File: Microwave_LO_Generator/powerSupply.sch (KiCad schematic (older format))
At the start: 26 parts, among them IC1 ADP150AUJZ-3.3-R7, U2 LM317L_SO8, U3 LM317L_SO8

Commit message: add vco
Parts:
- gave numbers to parts that had none: 3
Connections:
- net labels added: +5VA
- net labels removed: +5V
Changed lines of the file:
@@
 $Descr A4 11693 8268
 encoding utf-8
-Sheet 3 3
+Sheet 3 4
 Title ""
 Date ""
@@
 Wire Wire Line
 	5350 2000 5600 2000
-Wire Wire Line
-	5600 2000 5600 1950
 Connection ~ 5350 2000
 $Comp
@@
 	5600 3950 5600 3900
 Connection ~ 5350 3950
-$Comp
-L power:+5V #PWR0130
-U 1 1 5FC0CF33
-P 5600 1950
-F 0 "#PWR0130" H 5600 1800 50  0001 C CNN
-F 1 "+5V" H 5615 2123 50  0000 C CNN
-F 2 "" H 5600 1950 50  0001 C CNN
-F 3 "" H 5600 1950 50  0001 C CNN
-	1    5600 1950
-	1    0    0    -1
-$EndComp
 Wire Wire Line
 	1600 3600 1600 2000
@@
 AR Path="/5FBFBF42/5FC33DC2" Ref="C?"  Part="1"
 AR Path="/5FBD30A7/5FBFBF42/5FC33DC2" Ref="C?"  Part="1"
-AR Path="/5FBD5B32/5FC33DC2" Ref="C?"  Part="1"
-F 0 "C?" H 9535 2054 50  0000 R CNN
+AR Path="/5FBD5B32/5FC33DC2" Ref="C25"  Part="1"
+F 0 "C25" H 9535 2054 50  0000 R CNN
 F 1 "1u" H 9535 2145 50  0000 R CNN
 F 2 "Capacitor_SMD:C_0402_1005Metric_Pad0.74x0.62mm_HandSolder" H 9688 1950 50  0001 C CNN
@@
 $EndComp
 $Comp
-L pspice:0 #GND?
+L pspice:0 #GND0113
 U 1 1 5FC33DC8
 P 9650 2350
-F 0 "#GND?" H 9650 2250 50  0001 C CNN
+F 0 "#GND0113" H 9650 2250 50  0001 C CNN
 F 1 "0" H 9650 2439 50  0000 C CNN
 F 2 "" H 9650 2350 50  0001 C CNN
@@
 	9450 1800 9650 1800
 $Comp
-L Device:R R?
+L Device:R R13
 U 1 1 5FC3777E
 P 10100 2050
-F 0 "R?" H 10170 2096 50  0000 L CNN
+F 0 "R13" H 10170 2096 50  0000 L CNN
 F 1 "1K" H 10170 2005 50  0000 L CNN
 F 2 "" V 10030 2050 50  0001 C CNN
@@
 P 10100 2450
 AR Path="/5FBD30A7/5FBFBF42/5FC3CA84" Ref="D?"  Part="1"
-AR Path="/5FBD5B32/5FC3CA84" Ref="D?"  Part="1"
-F 0 "D?" V 10146 2322 50  0000 R CNN
+AR Path="/5FBD5B32/5FC3CA84" Ref="D7"  Part="1"
+F 0 "D7" V 10146 2322 50  0000 R CNN
 F 1 "DIODE" V 10055 2322 50  0000 R CNN
 F 2 "" H 10100 2450 50  0001 C CNN
@@
 $EndComp
 $Comp
-L pspice:0 #GND?
+L pspice:0 #GND0114
 U 1 1 5FC4242C
 P 10100 2650
-F 0 "#GND?" H 10100 2550 50  0001 C CNN
+F 0 "#GND0114" H 10100 2550 50  0001 C CNN
 F 1 "0" H 10100 2739 50  0000 C CNN
 F 2 "" H 10100 2650 50  0001 C CNN
@@
 Connection ~ 10100 1700
 $Comp
-L power:+5VD #PWR?
+L power:+5VD #PWR0132
 U 1 1 5FC480BB
 P 10400 1600
-F 0 "#PWR?" H 10400 1450 50  0001 C CNN
+F 0 "#PWR0132" H 10400 1450 50  0001 C CNN
 F 1 "+5VD" H 10415 1773 50  0000 C CNN
 F 2 "" H 10400 1600 50  0001 C CNN
@@
 	1    0    0    -1
 $EndComp
+$Comp
+L power:+5VA #PWR?
+U 1 1 5FCA5BC6
+P 5600 1800
+F 0 "#PWR?" H 5600 1650 50  0001 C CNN
+F 1 "+5VA" H 5615 1973 50  0000 C CNN
+F 2 "" H 5600 1800 50  0001 C CNN
+F 3 "" H 5600 1800 50  0001 C CNN
+	1    5600 1800
+	1    0    0    -1
+$EndComp
+Wire Wire Line
+	5600 2000 5600 1800
 $EndSCHEMATC

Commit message: Update and fix
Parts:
- removed D7: DIODE, symbol pspice:DIODE
- added D7: LED, LED_SMD:LED_0805_2012Metric_Pad1.15x1.40mm_HandSolder, symbol Device:LED
- C23: value 1u -> 4.7u
- C24: value 1u -> 100p
- D2, D3, D4, D5, D6: footprint (none) -> Diode_SMD:D_MELF
- R10, R11, R12, R13, R7, R8, R9: footprint (none) -> Resistor_SMD:R_0402_1005Metric_Pad0.72x0.64mm_HandSolder
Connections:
- net +5VD: no longer IC1.4 (NC), R13.1
- net 0: now also D7.1 (K)
- net +3V3: now reaches C25.2, IC1.5 (VOUT)
- net +3V3: now also R13.1
- net at R13.2: now also D7.2 (A)
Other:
- moved on the sheet: R13
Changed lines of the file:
@@
 F 0 "R7" V 2843 2000 50  0000 C CNN
 F 1 "0r" V 2934 2000 50  0000 C CNN
-F 2 "" V 2980 2000 50  0001 C CNN
+F 2 "Resistor_SMD:R_0402_1005Metric_Pad0.72x0.64mm_HandSolder" V 2980 2000 50  0001 C CNN
 F 3 "~" H 3050 2000 50  0001 C CNN
 	1    3050 2000
@@
 F 0 "R9" H 4920 2246 50  0000 L CNN
 F 1 "240r" H 4920 2155 50  0000 L CNN
-F 2 "" V 4780 2200 50  0001 C CNN
+F 2 "Resistor_SMD:R_0402_1005Metric_Pad0.72x0.64mm_HandSolder" V 4780 2200 50  0001 C CNN
 F 3 "~" H 4850 2200 50  0001 C CNN
 	1    4850 2200
@@
 F 0 "R10" H 4920 2646 50  0000 L CNN
 F 1 "720r" H 4920 2555 50  0000 L CNN
-F 2 "" V 4780 2600 50  0001 C CNN
+F 2 "Resistor_SMD:R_0402_1005Metric_Pad0.72x0.64mm_HandSolder" V 4780 2600 50  0001 C CNN
 F 3 "~" H 4850 2600 50  0001 C CNN
 	1    4850 2600
@@
 F 0 "D2" V 1096 3722 50  0000 R CNN
 F 1 "DIODE" V 1005 3722 50  0000 R CNN
-F 2 "" H 1050 3850 50  0001 C CNN
+F 2 "Diode_SMD:D_MELF" H 1050 3850 50  0001 C CNN
 F 3 "~" H 1050 3850 50  0001 C CNN
 	1    1050 3850
@@
 F 0 "D3" V 3946 1422 50  0000 R CNN
 F 1 "DIODE" V 3855 1422 50  0000 R CNN
-F 2 "" H 3900 1550 50  0001 C CNN
+F 2 "Diode_SMD:D_MELF" H 3900 1550 50  0001 C CNN
 F 3 "~" H 3900 1550 50  0001 C CNN
 	1    3900 1550
@@
 F 0 "D5" V 4446 2072 50  0000 R CNN
 F 1 "DIODE" V 4355 2072 50  0000 R CNN
-F 2 "" H 4400 2200 50  0001 C CNN
+F 2 "Diode_SMD:D_MELF" H 4400 2200 50  0001 C CNN
 F 3 "~" H 4400 2200 50  0001 C CNN
 	1    4400 2200
@@
 F 0 "R8" V 2843 3950 50  0000 C CNN
 F 1 "0r" V 2934 3950 50  0000 C CNN
-F 2 "" V 2980 3950 50  0001 C CNN
+F 2 "Resistor_SMD:R_0402_1005Metric_Pad0.72x0.64mm_HandSolder" V 2980 3950 50  0001 C CNN
 F 3 "~" H 3050 3950 50  0001 C CNN
 	1    3050 3950
@@
 F 0 "R11" H 4920 4196 50  0000 L CNN
 F 1 "240r" H 4920 4105 50  0000 L CNN
-F 2 "" V 4780 4150 50  0001 C CNN
+F 2 "Resistor_SMD:R_0402_1005Metric_Pad0.72x0.64mm_HandSolder" V 4780 4150 50  0001 C CNN
 F 3 "~" H 4850 4150 50  0001 C CNN
 	1    4850 4150
@@
 F 0 "R12" H 4920 4596 50  0000 L CNN
 F 1 "1K488" H 4920 4505 50  0000 L CNN
-F 2 "" V 4780 4550 50  0001 C CNN
+F 2 "Resistor_SMD:R_0402_1005Metric_Pad0.72x0.64mm_HandSolder" V 4780 4550 50  0001 C CNN
 F 3 "~" H 4850 4550 50  0001 C CNN
 	1    4850 4550
@@
 F 0 "D4" V 3946 3372 50  0000 R CNN
 F 1 "DIODE" V 3855 3372 50  0000 R CNN
-F 2 "" H 3900 3500 50  0001 C CNN
+F 2 "Diode_SMD:D_MELF" H 3900 3500 50  0001 C CNN
 F 3 "~" H 3900 3500 50  0001 C CNN
 	1    3900 3500
@@
 F 0 "D6" V 4446 4022 50  0000 R CNN
 F 1 "DIODE" V 4355 4022 50  0000 R CNN
-F 2 "" H 4400 4150 50  0001 C CNN
+F 2 "Diode_SMD:D_MELF" H 4400 4150 50  0001 C CNN
 F 3 "~" H 4400 4150 50  0001 C CNN
 	1    4400 4150
@@
 AR Path="/5FBD5B32/5FC10CCE" Ref="C23"  Part="1"
 F 0 "C23" H 6685 1854 50  0000 R CNN
-F 1 "1u" H 6685 1945 50  0000 R CNN
+F 1 "4.7u" H 6685 1945 50  0000 R CNN
 F 2 "Capacitor_SMD:C_0402_1005Metric_Pad0.74x0.62mm_HandSolder" H 6838 1750 50  0001 C CNN
 F 3 "~" H 6800 1900 50  0001 C CNN
@@
 AR Path="/5FBD5B32/5FC1C79A" Ref="C24"  Part="1"
 F 0 "C24" H 7685 2004 50  0000 R CNN
-F 1 "1u" H 7685 2095 50  0000 R CNN
+F 1 "100p" H 7685 2095 50  0000 R CNN
 F 2 "Capacitor_SMD:C_0402_1005Metric_Pad0.74x0.62mm_HandSolder" H 7838 1900 50  0001 C CNN
 F 3 "~" H 7800 2050 50  0001 C CNN
@@
 L Device:R R13
 U 1 1 5FC3777E
-P 10100 2050
-F 0 "R13" H 10170 2096 50  0000 L CNN
-F 1 "1K" H 10170 2005 50  0000 L CNN
-F 2 "" V 10030 2050 50  0001 C CNN
-F 3 "~" H 10100 2050 50  0001 C CNN
-	1    10100 2050
-	1    0    0    -1
-$EndComp
-$Comp
-L pspice:DIODE D?
-U 1 1 5FC3CA84
-P 10100 2450
-AR Path="/5FBD30A7/5FBFBF42/5FC3CA84" Ref="D?"  Part="1"
-AR Path="/5FBD5B32/5FC3CA84" Ref="D7"  Part="1"
-F 0 "D7" V 10146 2322 50  0000 R CNN
-F 1 "DIODE" V 10055 2322 50  0000 R CNN
-F 2 "" H 10100 2450 50  0001 C CNN
-F 3 "~" H 10100 2450 50  0001 C CNN
-	1    10100 2450
-	0    1    1    0
+P 10100 2150
+F 0 "R13" H 10170 2196 50  0000 L CNN
+F 1 "1K" H 10170 2105 50  0000 L CNN
+F 2 "Resistor_SMD:R_0402_1005Metric_Pad0.72x0.64mm_HandSolder" V 10030 2150 50  0001 C CNN
+F 3 "~" H 10100 2150 50  0001 C CNN
+	1    10100 2150
+	1    0    0    -1
 $EndComp
 $Comp
 L pspice:0 #GND0114
 U 1 1 5FC4242C
-P 10100 2650
-F 0 "#GND0114" H 10100 2550 50  0001 C CNN
-F 1 "0" H 10100 2739 50  0000 C CNN
-F 2 "" H 10100 2650 50  0001 C CNN
-F 3 "~" H 10100 2650 50  0001 C CNN
-	1    10100 2650
-	1    0    0    -1
-$EndComp
-Wire Wire Line
-	10100 2250 10100 2200
-Wire Wire Line
-	10100 1900 10100 1700
-Wire Wire Line
-	10100 1700 9450 1700
-Wire Wire Line
-	10100 1700 10400 1700
-Wire Wire Line
-	10400 1700 10400 1600
-Connection ~ 10100 1700
-$Comp
-L power:+5VD #PWR0132
-U 1 1 5FC480BB
-P 10400 1600
-F 0 "#PWR0132" H 10400 1450 50  0001 C CNN
-F 1 "+5VD" H 10415 1773 50  0000 C CNN
-F 2 "" H 10400 1600 50  0001 C CNN
-F 3 "" H 10400 1600 50  0001 C CNN
-	1    10400 1600
-	1    0    0    -1
-$EndComp
-$Comp
-L power:+5VA #PWR?
+P 10100 2750
+F 0 "#GND0114" H 10100 2650 50  0001 C CNN
+F 1 "0" H 10100 2839 50  0000 C CNN
+F 2 "" H 10100 2750 50  0001 C CNN
+F 3 "~" H 10100 2750 50  0001 C CNN
+	1    10100 2750
+	1    0    0    -1
+$EndComp
+Wire Wire Line
+	10100 2350 10100 2300
+Wire Wire Line
+	10100 2000 10100 1800
+Wire Wire Line
+	10100 1800 10400 1800
+Wire Wire Line
+	10400 1800 10400 1700
+$Comp
+L power:+5VA #PWR0130
 U 1 1 5FCA5BC6
 P 5600 1800
-F 0 "#PWR?" H 5600 1650 50  0001 C CNN
+F 0 "#PWR0130" H 5600 1650 50  0001 C CNN
 F 1 "+5VA" H 5615 1973 50  0000 C CNN
 F 2 "" H 5600 1800 50  0001 C CNN
@@
 Wire Wire Line
 	5600 2000 5600 1800
+$Comp
+L Device:LED D?
+U 1 1 5FBF769A
+P 10100 2500
+AR Path="/5FBD30A7/5FBF769A" Ref="D?"  Part="1"
+AR Path="/5FBD5B32/5FBF769A" Ref="D7"  Part="1"
+F 0 "D7" V 10139 2382 50  0000 R CNN
+F 1 "LED" V 10048 2382 50  0000 R CNN
+F 2 "LED_SMD:LED_0805_2012Metric_Pad1.15x1.40mm_HandSolder" H 10100 2500 50  0001 C CNN
+F 3 "https://www.mouser.it/datasheet/2/678/av02-0551en-ds-hsmx-cxxx-05mar2012-1827675.pdf" H 10100 2500 50  0001 C CNN
+F 4 "HSMG-C170" H 10100 2500 50  0001 C CNN "Manufacturer/Part Number"
+F 5 "Mouser 630-HSMG-C170" H 10100 2500 50  0001 C CNN "Supplier Stock Code"
+	1    10100 2500
+	0    -1   -1   0
+$EndComp
+Wire Wire Line
+	10100 2650 10100 2750
+Wire Wire Line
+	9650 1800 10100 1800
+Connection ~ 9650 1800
+Connection ~ 10100 1800
+$Comp
+L power:+3.3V #PWR0132
+U 1 1 5FC7592E
+P 10400 1700
+F 0 "#PWR0132" H 10400 1550 50  0001 C CNN
+F 1 "+3.3V" H 10415 1873 50  0000 C CNN
+F 2 "" H 10400 1700 50  0001 C CNN
+F 3 "" H 10400 1700 50  0001 C CNN
+	1    10400 1700
+	1    0    0    -1
+$EndComp
 $EndSCHEMATC

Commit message: Power Supply update
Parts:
- removed C18, C20: 1u, Capacitor_SMD:C_0402_1005Metric_Pad0.74x0.62mm_HandSolder, symbol Device:C
- removed D3, D4, D5, D6: DIODE, Diode_SMD:D_MELF, symbol pspice:DIODE
- removed IC1: ADP150AUJZ-3.3-R7, SamacSys_Parts:SOT95P280X100-5N, symbol SamacSys_Parts:ADP150AUJZ-3.3-R7
- removed R10: 720r, Resistor_SMD:R_0402_1005Metric_Pad0.72x0.64mm_HandSolder, symbol Device:R
- removed R7: 0r, Resistor_SMD:R_0402_1005Metric_Pad0.72x0.64mm_HandSolder, symbol Device:R
- removed R9: 240r, Resistor_SMD:R_0402_1005Metric_Pad0.72x0.64mm_HandSolder, symbol Device:R
- removed U2, U3: LM317L_SO8, Package_SO:SOIC-8_3.9x4.9mm_P1.27mm, symbol Regulator_Linear:LM317L_SO8
- added C3, C31, C5: 100p, Capacitor_SMD:C_0402_1005Metric_Pad0.74x0.62mm_HandSolder, symbol Device:C
- added C32, C33, C34: 10n, Capacitor_SMD:C_0402_1005Metric_Pad0.74x0.62mm_HandSolder, symbol Device:C
- added C35, C36: 3.3u, Capacitor_SMD:C_0402_1005Metric_Pad0.74x0.62mm_HandSolder, symbol Device:C
- added J1, J?: Conn_01x02_Male, Connector_PinHeader_2.54mm:PinHeader_1x02_P2.54mm_Vertical, symbol Connector:Conn_01x02_Male
- added U2: LT1962-3.3, Package_SO:MSOP-8_3x3mm_P0.65mm, symbol Regulator_Linear:LT1962-3.3
- added U3: LT3010, Package_SO:MSOP-8-1EP_3x3mm_P0.65mm_EP1.68x1.88mm, symbol Regulator_Linear:LT3010
- added U5, U6: LT1962-5, Package_SO:MSOP-8_3x3mm_P0.65mm, symbol Regulator_Linear:LT1962-5
- C17, C19: value 1u -> 4.7u
- C21: value 1u -> 100p
- C25: value 1u -> 3.3u
- R11: value 240r -> 1K8
- R12: value 1K488 -> 300r
- R8: value 0r -> 10r
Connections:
- net +12V: now also J1.1 (Pin_1); no longer C16.2
- net +3V3: now also C32.2, U2.1 (OUT), U2.2 (SENSE)
- net +5VA: now also C33.2, C35.2, U5.1 (OUT), U5.2 (SENSE); no longer C21.2
- net +5VD: now also C34.2, C36.2, U6.1 (OUT), U6.2 (SENSE); no longer C23.2, C24.2
- net +9V: now also C5.2, U3.1 (OUT)
- net 0: now also C3.1, C31.1, C35.1, C36.1, J1.2 (Pin_2), J?.2 (Pin_2), U2.4 (GND), U3.4 (GND), U3.9 (GND), U5.4 (GND), U6.4 (GND)
- net +6V: now reaches C17.2
- net +6V: now also C19.2, C21.2, C23.2, C24.2, C31.2, J?.1 (Pin_1), U2.5 (~SHDN), U2.8 (IN), U5.5 (~SHDN), U5.8 (IN), U6.5 (~SHDN), U6.8 (IN)
- net at R8.1: now also C16.2, C3.2, U3.5 (~SHDN), U3.8 (IN)
- net at R11.2, R12.1: now also C5.1, U3.2 (ADJ)
- new net: C32.1, U2.3 (BYP)
- new net: C33.1, U5.3 (BYP)
- new net: C34.1, U6.3 (BYP)
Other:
- moved on the sheet: C16, C22, C23, C25, D2, D7, R11, R12, R13, R8

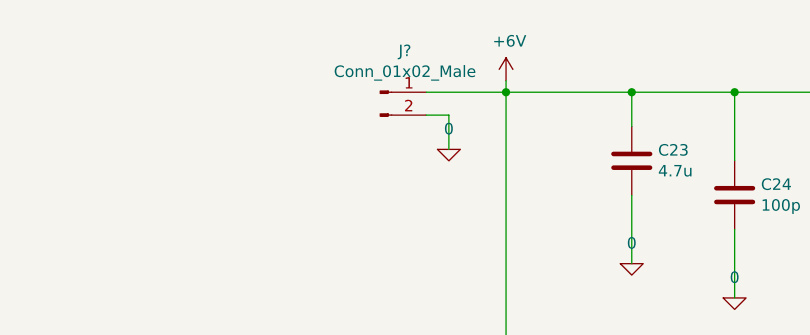
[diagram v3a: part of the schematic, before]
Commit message: Add RF/2
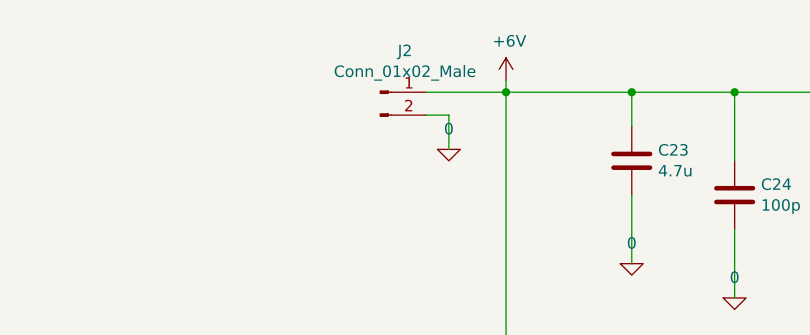
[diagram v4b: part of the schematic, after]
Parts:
- gave numbers to parts that had none: 1
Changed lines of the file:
@@
 	1550 4200 1550 4150
 $Comp
-L Connector:Conn_01x02_Male J?
+L Connector:Conn_01x02_Male J2
 U 1 1 5FDB237F
 P 6250 1600
-F 0 "J?" H 6358 1781 50  0000 C CNN
+F 0 "J2" H 6358 1781 50  0000 C CNN
 F 1 "Conn_01x02_Male" H 6358 1690 50  0000 C CNN
 F 2 "Connector_PinHeader_2.54mm:PinHeader_1x02_P2.54mm_Vertical" H 6250 1600 50  0001 C CNN
@@
 	6800 1600 6800 3200
 $Comp
-L pspice:0 #GND?
+L pspice:0 #GND0129
 U 1 1 5FDBD0D5
 P 6550 1850
-F 0 "#GND?" H 6550 1750 50  0001 C CNN
+F 0 "#GND0129" H 6550 1750 50  0001 C CNN
 F 1 "0" H 6550 1939 50  0000 C CNN
 F 2 "" H 6550 1850 50  0001 C CNN

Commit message: A lot of change
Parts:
- added D?: DIODE, Diode_SMD:D_MELF, symbol pspice:DIODE
- added TP3, TP4, TP5, TP6: TestPoint, TestPoint:TestPoint_Loop_D2.60mm_Drill1.6mm_Beaded, symbol frequencySynthesizer-rescue:TestPoint-frequencySintesizer
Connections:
- net +3V3: now also TP6.1
- net +5VA: now also TP4.1
- net +5VD: now also TP5.1
- net +6V: now also D?.2 (A)
- net +9V: now also TP3.1
- net 0: now also D?.1 (K)
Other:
- moved on the sheet: J2
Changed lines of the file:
@@
 L power:+9V #PWR0129
 U 1 1 5FC0B368
-P 5150 3650
-F 0 "#PWR0129" H 5150 3500 50  0001 C CNN
-F 1 "+9V" H 5165 3823 50  0000 C CNN
-F 2 "" H 5150 3650 50  0001 C CNN
-F 3 "" H 5150 3650 50  0001 C CNN
-	1    5150 3650
-	1    0    0    -1
-$EndComp
-Wire Wire Line
-	4900 3700 5150 3700
-Wire Wire Line
-	5150 3700 5150 3650
+P 5350 3650
+F 0 "#PWR0129" H 5350 3500 50  0001 C CNN
+F 1 "+9V" H 5365 3823 50  0000 C CNN
+F 2 "" H 5350 3650 50  0001 C CNN
+F 3 "" H 5350 3650 50  0001 C CNN
+	1    5350 3650
+	1    0    0    -1
+$EndComp
+Wire Wire Line
+	5350 3700 5350 3650
 $Comp
 L Device:C C?
@@
 L Connector:Conn_01x02_Male J2
 U 1 1 5FDB237F
-P 6250 1600
-F 0 "J2" H 6358 1781 50  0000 C CNN
-F 1 "Conn_01x02_Male" H 6358 1690 50  0000 C CNN
-F 2 "Connector_PinHeader_2.54mm:PinHeader_1x02_P2.54mm_Vertical" H 6250 1600 50  0001 C CNN
-F 3 "~" H 6250 1600 50  0001 C CNN
-	1    6250 1600
-	1    0    0    -1
-$EndComp
-Wire Wire Line
-	6450 1600 6800 1600
+P 5550 1600
+F 0 "J2" H 5658 1781 50  0000 C CNN
+F 1 "Conn_01x02_Male" H 5658 1690 50  0000 C CNN
+F 2 "Connector_PinHeader_2.54mm:PinHeader_1x02_P2.54mm_Vertical" H 5550 1600 50  0001 C CNN
+F 3 "~" H 5550 1600 50  0001 C CNN
+	1    5550 1600
+	1    0    0    -1
+$EndComp
 Wire Wire Line
 	6800 1600 6800 3200
@@
 L pspice:0 #GND0129
 U 1 1 5FDBD0D5
-P 6550 1850
-F 0 "#GND0129" H 6550 1750 50  0001 C CNN
-F 1 "0" H 6550 1939 50  0000 C CNN
-F 2 "" H 6550 1850 50  0001 C CNN
-F 3 "~" H 6550 1850 50  0001 C CNN
-	1    6550 1850
-	1    0    0    -1
-$EndComp
-Wire Wire Line
-	6550 1850 6550 1700
-Wire Wire Line
-	6550 1700 6450 1700
+P 5850 1850
+F 0 "#GND0129" H 5850 1750 50  0001 C CNN
+F 1 "0" H 5850 1939 50  0000 C CNN
+F 2 "" H 5850 1850 50  0001 C CNN
+F 3 "~" H 5850 1850 50  0001 C CNN
+	1    5850 1850
+	1    0    0    -1
+$EndComp
+Wire Wire Line
+	5850 1850 5850 1700
+Wire Wire Line
+	5850 1700 5750 1700
+$Comp
+L frequencySynthesizer-rescue:TestPoint-frequencySintesizer TP?
+U 1 1 5FDAD9C9
+P 4900 3600
+AR Path="/5FBD30A7/5FDAD9C9" Ref="TP?"  Part="1"
+AR Path="/5FBD5B32/5FDAD9C9" Ref="TP3"  Part="1"
+F 0 "TP3" H 4958 3718 50  0000 L CNN
+F 1 "TestPoint" H 4958 3627 50  0000 L CNN
+F 2 "TestPoint:TestPoint_Loop_D2.60mm_Drill1.6mm_Beaded" H 5100 3600 50  0001 C CNN
+F 3 "https://www.mouser.it/datasheet/2/215/005-5009-741293.pdf" H 5100 3600 50  0001 C CNN
+F 4 "5007" H 4900 3600 50  0001 C CNN "Manufacturer/Part Number"
+F 5 "Mouser 534-5007" H 4900 3600 50  0001 C CNN "Supplier Stock Code"
+	1    4900 3600
+	1    0    0    -1
+$EndComp
+$Comp
+L frequencySynthesizer-rescue:TestPoint-frequencySintesizer TP?
+U 1 1 5FDB1936
+P 10250 1500
+AR Path="/5FBD30A7/5FDB1936" Ref="TP?"  Part="1"
+AR Path="/5FBD5B32/5FDB1936" Ref="TP6"  Part="1"
+F 0 "TP6" H 10308 1618 50  0000 L CNN
+F 1 "TestPoint" H 10308 1527 50  0000 L CNN
+F 2 "TestPoint:TestPoint_Loop_D2.60mm_Drill1.6mm_Beaded" H 10450 1500 50  0001 C CNN
+F 3 "https://www.mouser.it/datasheet/2/215/005-5009-741293.pdf" H 10450 1500 50  0001 C CNN
+F 4 "5007" H 10250 1500 50  0001 C CNN "Manufacturer/Part Number"
+F 5 "Mouser 534-5007" H 10250 1500 50  0001 C CNN "Supplier Stock Code"
+	1    10250 1500
+	1    0    0    -1
+$EndComp
+$Comp
+L frequencySynthesizer-rescue:TestPoint-frequencySintesizer TP?
+U 1 1 5FDB5D55
+P 9900 3100
+AR Path="/5FBD30A7/5FDB5D55" Ref="TP?"  Part="1"
+AR Path="/5FBD5B32/5FDB5D55" Ref="TP4"  Part="1"
+F 0 "TP4" H 9958 3218 50  0000 L CNN
+F 1 "TestPoint" H 9958 3127 50  0000 L CNN
+F 2 "TestPoint:TestPoint_Loop_D2.60mm_Drill1.6mm_Beaded" H 10100 3100 50  0001 C CNN
+F 3 "https://www.mouser.it/datasheet/2/215/005-5009-741293.pdf" H 10100 3100 50  0001 C CNN
+F 4 "5007" H 9900 3100 50  0001 C CNN "Manufacturer/Part Number"
+F 5 "Mouser 534-5007" H 9900 3100 50  0001 C CNN "Supplier Stock Code"
+	1    9900 3100
+	1    0    0    -1
+$EndComp
+$Comp
+L frequencySynthesizer-rescue:TestPoint-frequencySintesizer TP?
+U 1 1 5FDB9CE2
+P 9900 4400
+AR Path="/5FBD30A7/5FDB9CE2" Ref="TP?"  Part="1"
+AR Path="/5FBD5B32/5FDB9CE2" Ref="TP5"  Part="1"
+F 0 "TP5" H 9958 4518 50  0000 L CNN
+F 1 "TestPoint" H 9958 4427 50  0000 L CNN
+F 2 "TestPoint:TestPoint_Loop_D2.60mm_Drill1.6mm_Beaded" H 10100 4400 50  0001 C CNN
+F 3 "https://www.mouser.it/datasheet/2/215/005-5009-741293.pdf" H 10100 4400 50  0001 C CNN
+F 4 "5007" H 9900 4400 50  0001 C CNN "Manufacturer/Part Number"
+F 5 "Mouser 534-5007" H 9900 4400 50  0001 C CNN "Supplier Stock Code"
+	1    9900 4400
+	1    0    0    -1
+$EndComp
+Wire Wire Line
+	4900 3600 4900 3700
+Wire Wire Line
+	4900 3700 5350 3700
+Wire Wire Line
+	10250 1500 10250 1600
+Wire Wire Line
+	9900 3100 9900 3200
+Wire Wire Line
+	9900 4400 9900 4500
+$Comp
+L pspice:DIODE D?
+U 1 1 5FE480F6
+P 6300 1850
+AR Path="/5FBD30A7/5FBFBF42/5FE480F6" Ref="D?"  Part="1"
+AR Path="/5FBD5B32/5FE480F6" Ref="D?"  Part="1"
+F 0 "D?" V 6346 1722 50  0000 R CNN
+F 1 "DIODE" V 6255 1722 50  0000 R CNN
+F 2 "Diode_SMD:D_MELF" H 6300 1850 50  0001 C CNN
+F 3 "~" H 6300 1850 50  0001 C CNN
+	1    6300 1850
+	0    -1   -1   0
+$EndComp
+Wire Wire Line
+	5750 1600 6300 1600
+Wire Wire Line
+	6300 1650 6300 1600
+Connection ~ 6300 1600
+Wire Wire Line
+	6300 1600 6800 1600
+$Comp
+L pspice:0 #GND?
+U 1 1 5FE58A98
+P 6300 2300
+F 0 "#GND?" H 6300 2200 50  0001 C CNN
+F 1 "0" H 6300 2389 50  0000 C CNN
+F 2 "" H 6300 2300 50  0001 C CNN
+F 3 "~" H 6300 2300 50  0001 C CNN
+	1    6300 2300
+	1    0    0    -1
+$EndComp
+Wire Wire Line
+	6300 2050 6300 2300
 $EndSCHEMATC
